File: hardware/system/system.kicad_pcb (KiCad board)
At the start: 2 copper layers, 226.6 x 87.2 mm, 46 parts, among them J1 CART_SOCKET_28P, J2 EXTENSION PINS, SW1 POWER, SW2 RESET, SW3 A, SW4 B, SW5 UP, SW6 DN, SW7 LF, SW8 RT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

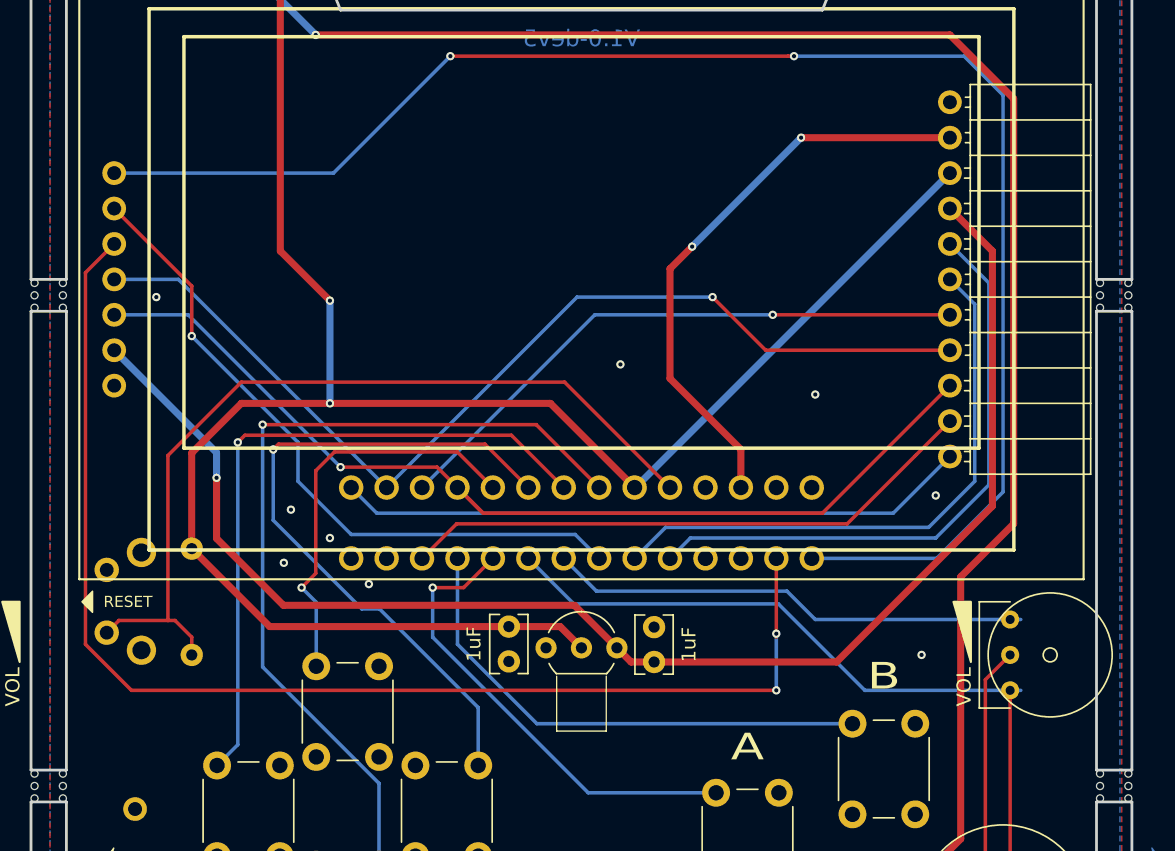
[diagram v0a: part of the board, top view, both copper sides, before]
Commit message: Remove 3.3V regulator
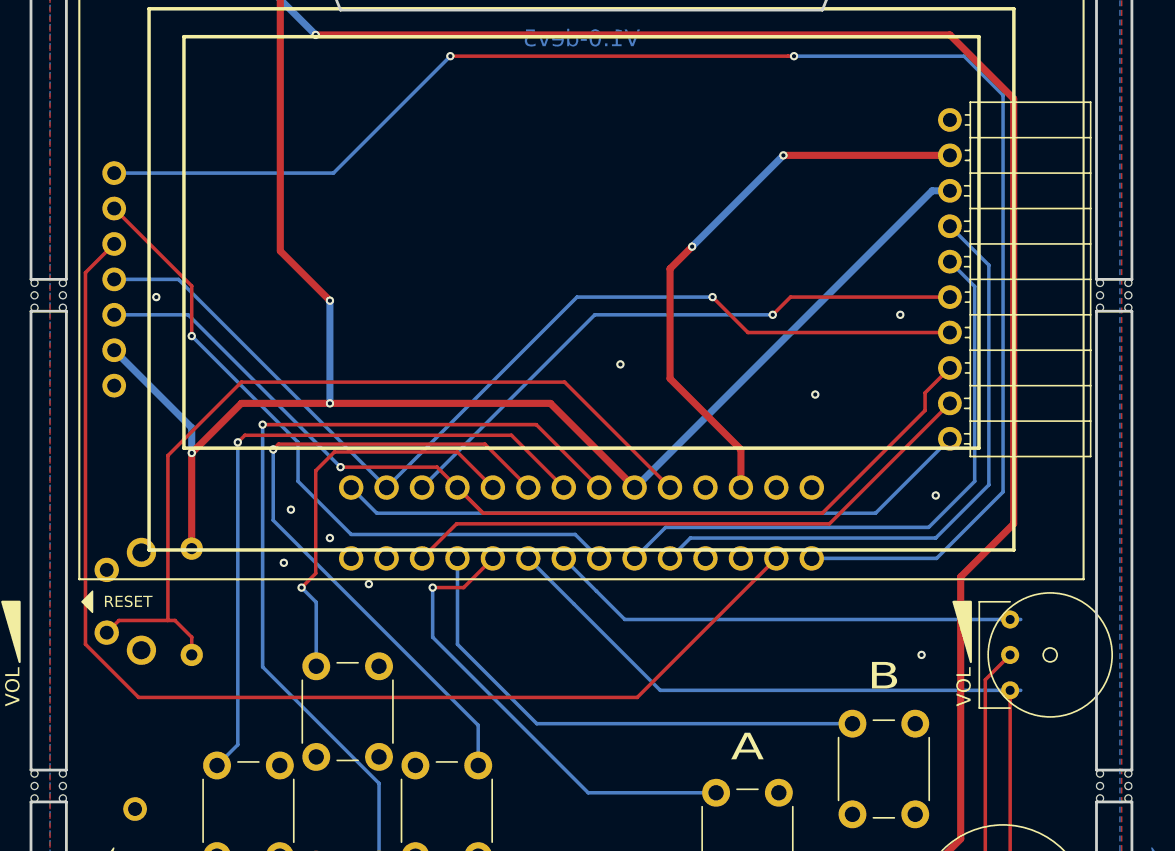
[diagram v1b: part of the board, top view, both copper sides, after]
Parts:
- removed C1, C2: 1uF, Capacitor_THT:C_Rect_L4.0mm_W2.5mm_P2.50mm
- removed the U2 at (139.7, 121.4)
- J2: value EXTENSION PINS -> EXT_PINS
- renumbered U3 to U2
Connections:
- J2 pad 10: D9_A9 -> D10_A10
- J2 pad 4: 3V3 -> SDA
- J2 pad 5: SDA -> SCL
- J2 pad 6: SCL -> MISO
- J2 pad 7: MISO -> MOSI
- J2 pad 8: MOSI -> SCK
- J2 pad 9: SCK -> D9_A9
- U2 pad 2: 3V3 -> VCC
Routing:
- net 3V3: track 103.1 -> 0.00 mm, vias 1 -> 0
- net VCC: track 141.6 -> 119.9 mm, vias 2 -> 3
- net Net-(J1-Pad2): track 89.9 -> 84.8 mm, vias 2 -> 0
- net SCL: track 41.9 -> 43.2 mm
- net SCK: track 72.2 -> 73.5 mm
- net SDA: track 43.5 -> 44.7 mm
- net Net-(J1-Pad20): track 49.2 -> 48.5 mm
- net RAW: track 41.7 -> 41.2 mm
- net MISO: track 43.0 -> 43.5 mm
- net D9_A9: track 41.9 -> 42.4 mm
- net D10_A10: track 45.4 -> 45.9 mm
- net MOSI: track 73.3 -> 72.8 mm
- net GND: vias 9 -> 10

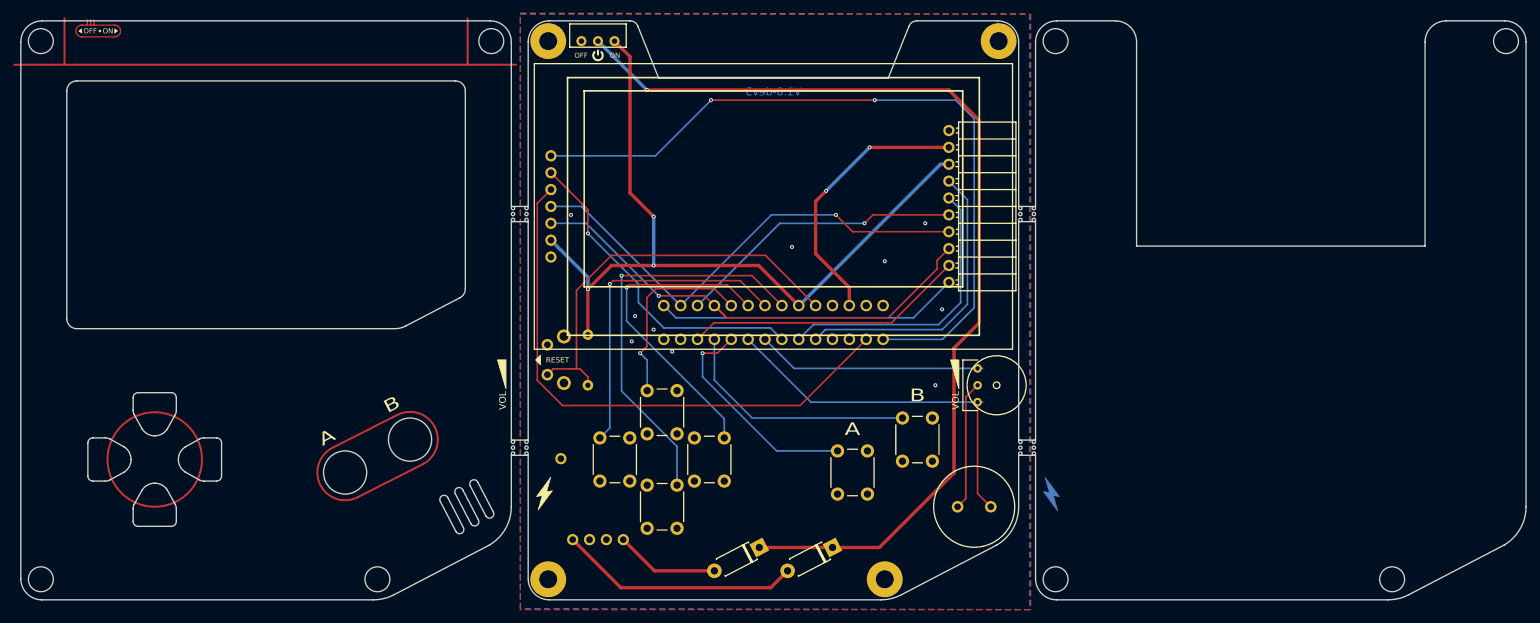
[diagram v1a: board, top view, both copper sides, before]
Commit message: Rename to dotMG
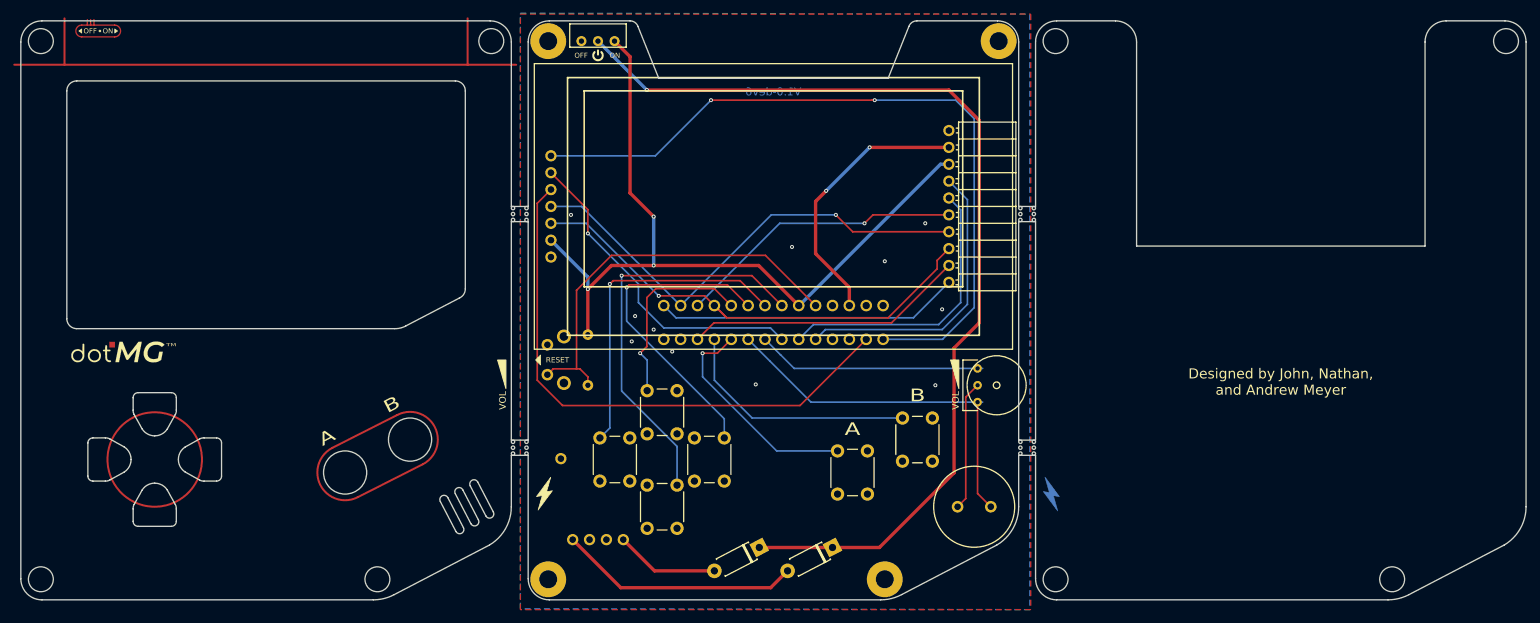
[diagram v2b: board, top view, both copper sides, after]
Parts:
- added G***: LOGO, system:LOGO, F.Cu at (40.1, 115.8)
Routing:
- net GND: vias 10 -> 11
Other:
- board text added: "V1.0-dev6"
- board text added: "github.com/menehune23/arduboy-dotmg"
- board text removed: "Arduboy CE"
- board text removed: "V1.0-dev5"
- board text removed: "github.com/menehune23/arduboy-ce"

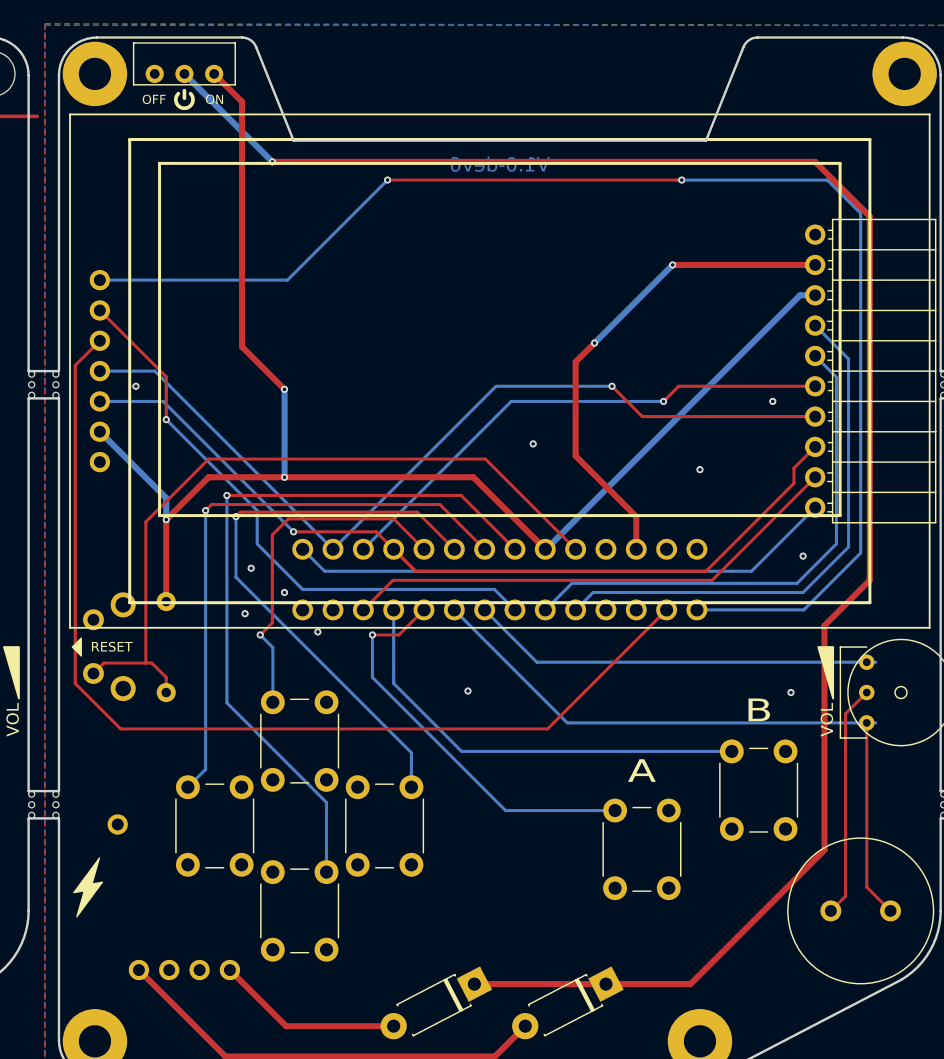
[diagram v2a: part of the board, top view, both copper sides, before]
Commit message: Move power/reset buttons inward slightly
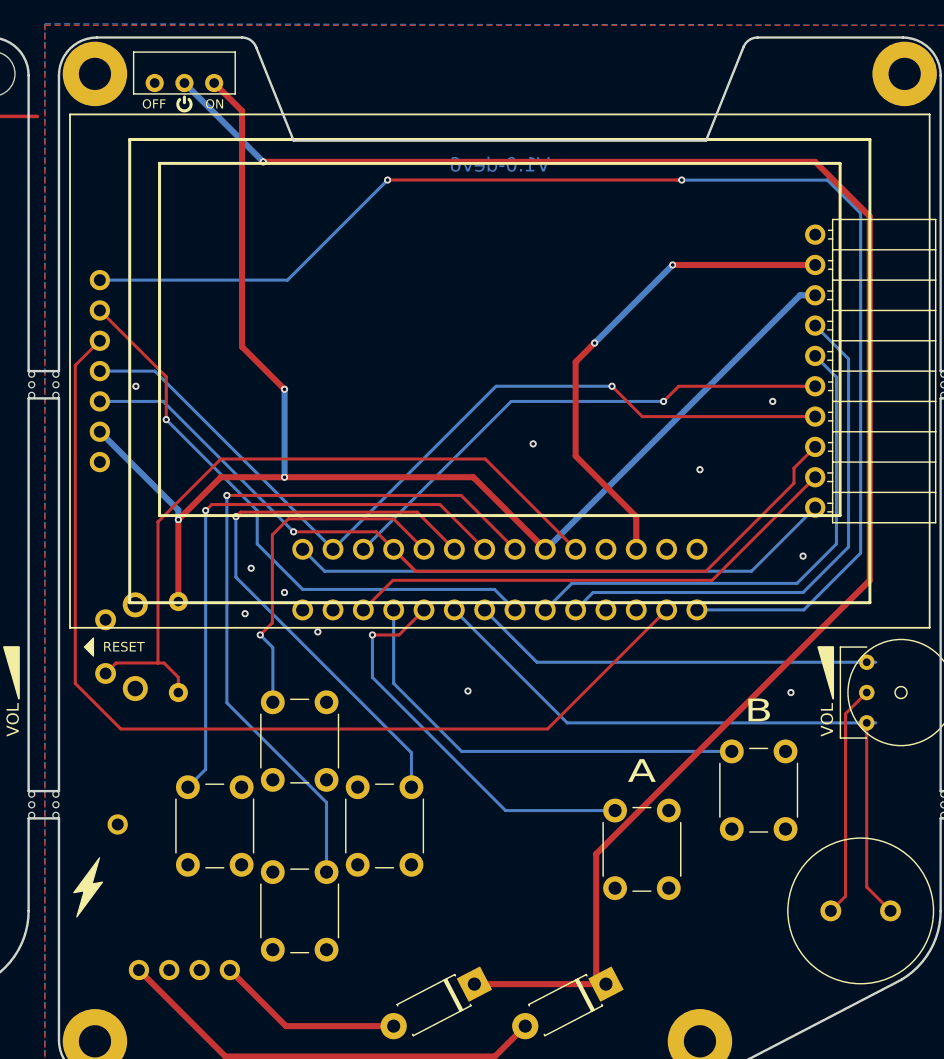
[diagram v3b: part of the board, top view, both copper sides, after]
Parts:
- moved SW2 1.02 mm to (106.7, 115.8)
- moved R1 1.02 mm to (112.8, 114.3)
- moved SW1 0.76 mm to (113.3, 70.9)
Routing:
- net Net-(D1-Pad1): track 151.0 -> 147.2 mm
- net VCC: track 119.9 -> 118.5 mm
- net Net-(J1-Pad24): track 61.4 -> 60.3 mm

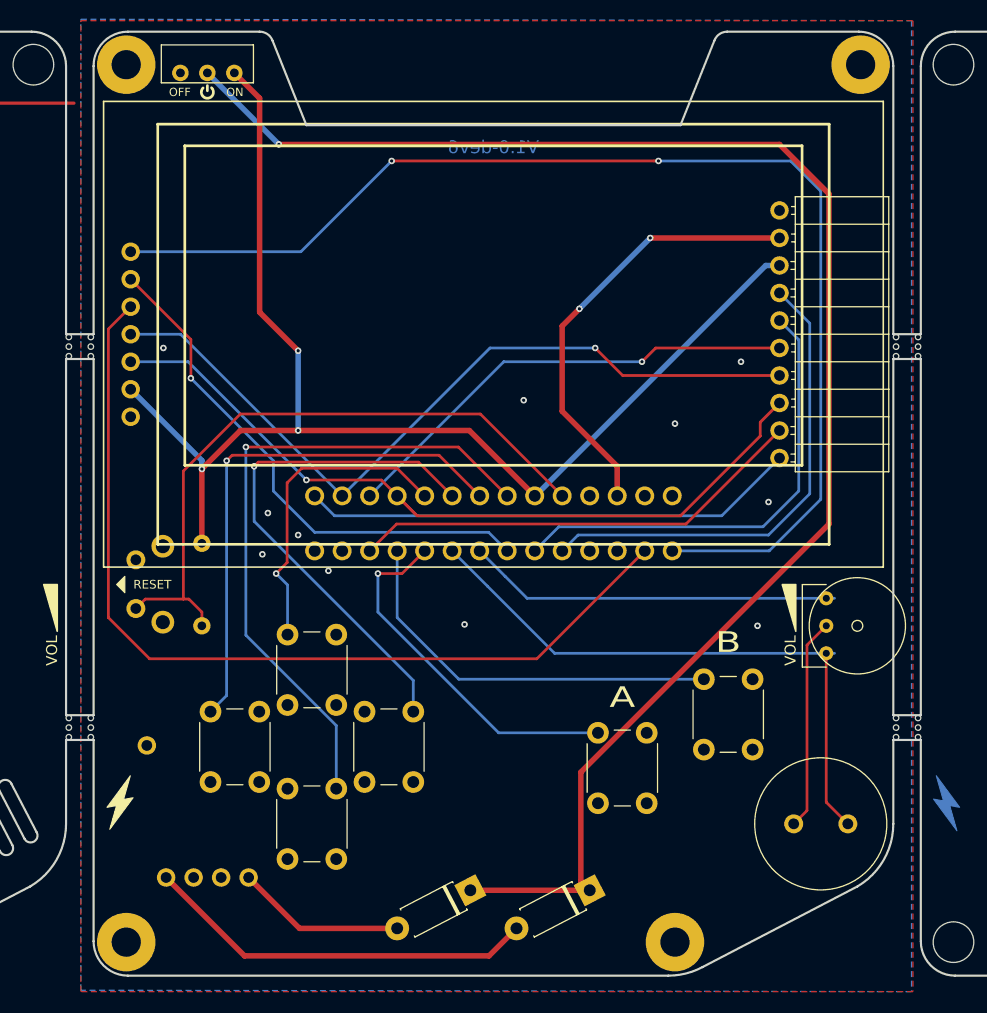
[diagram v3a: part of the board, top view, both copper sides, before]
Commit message: Minor board updates
- Add logo to main board
- Increase breakaway tab width (better for fabs)
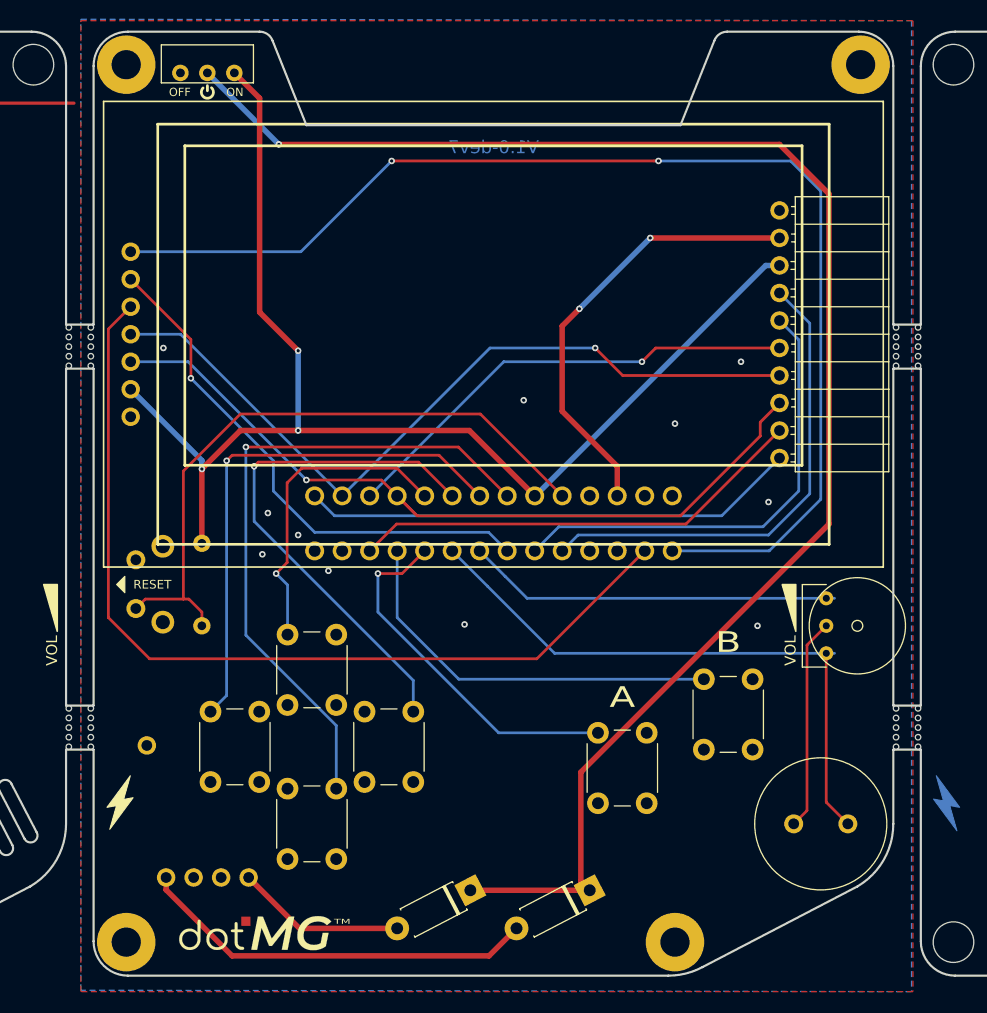
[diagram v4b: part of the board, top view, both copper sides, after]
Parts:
- added G***: LOGO, system:LOGO, F.Cu at (116.8, 149.2)
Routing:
- net Net-(D1-Pad2): track 36.4 -> 37.1 mm
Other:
- outline, holes or cut-outs redrawn
- board text added: "V1.0-dev7"
- board text removed: "V1.0-dev6"
